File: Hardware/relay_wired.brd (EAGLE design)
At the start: 100 x 80 mm, 9 parts, among them K1 JJM1-12V

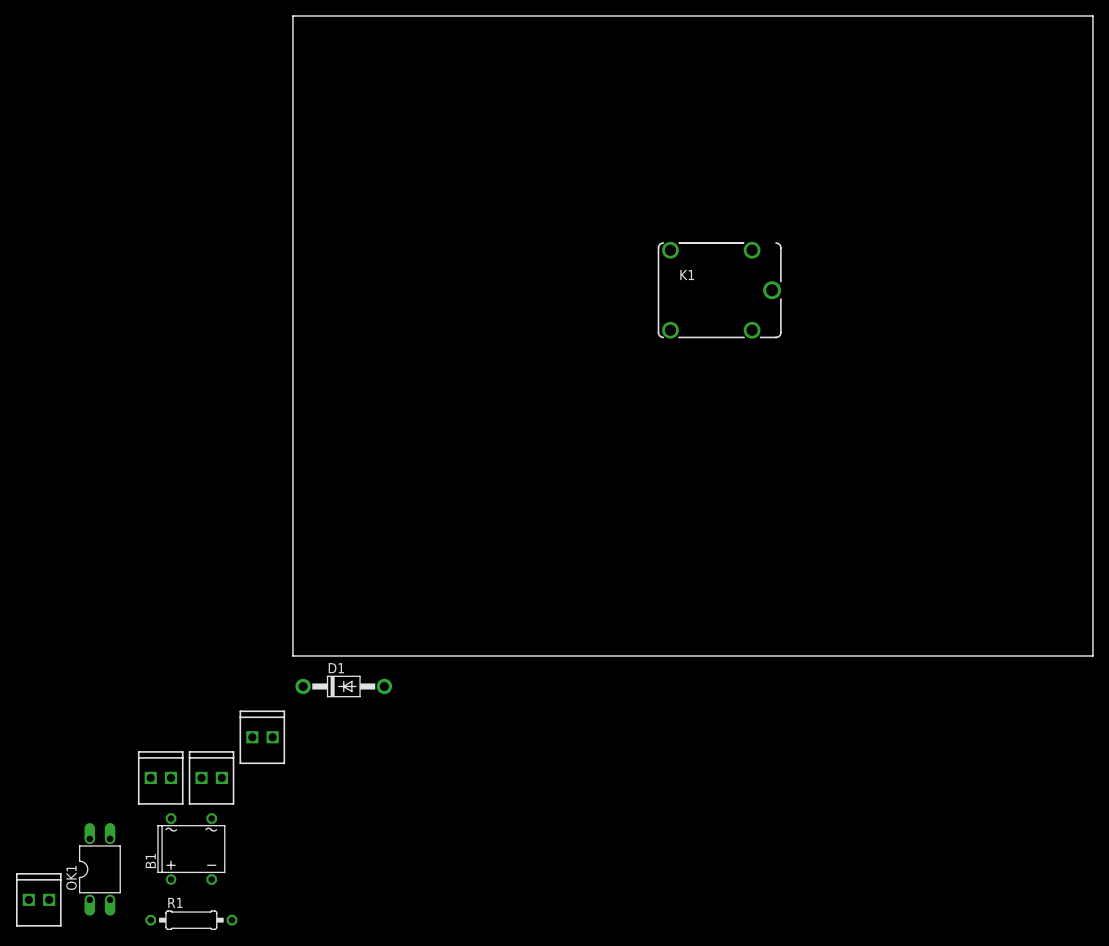
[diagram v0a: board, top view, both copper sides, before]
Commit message: Layout of board 33 x 33
Layout 33 x 33 board
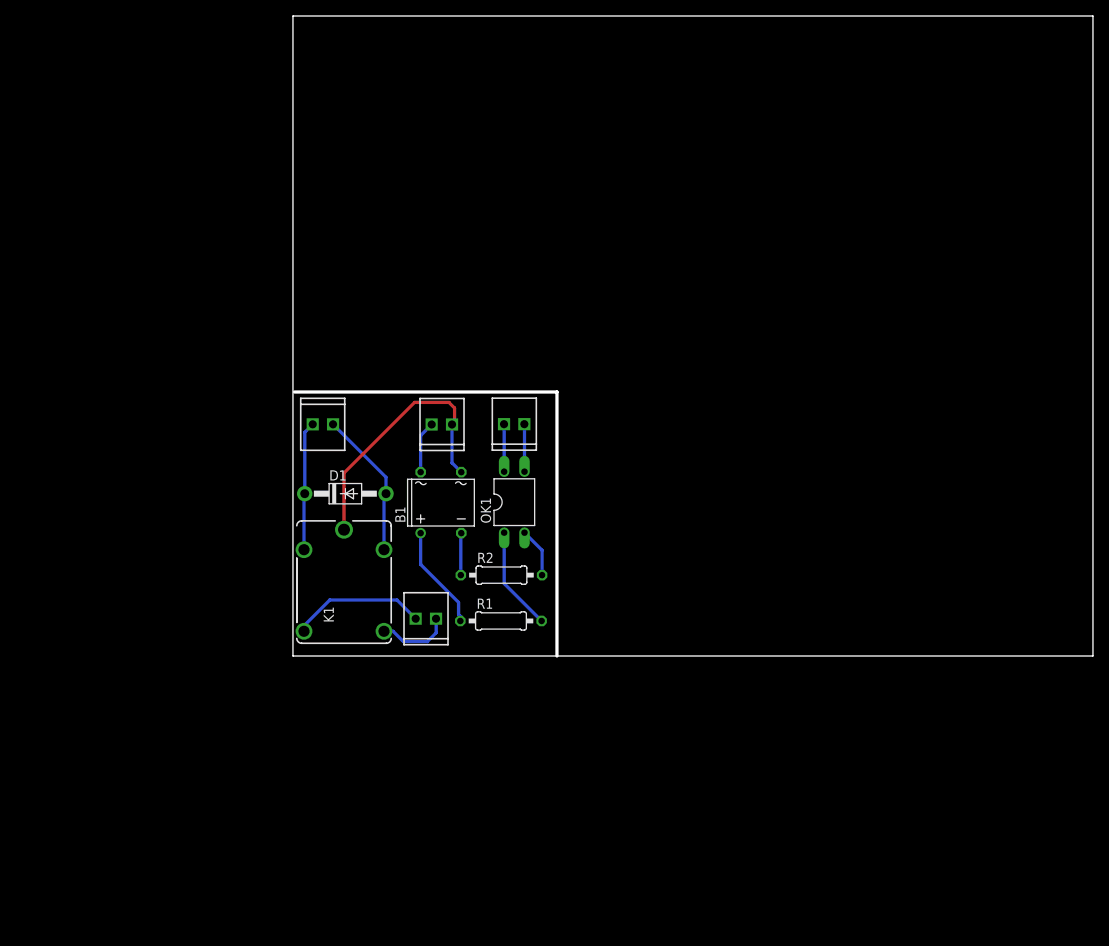
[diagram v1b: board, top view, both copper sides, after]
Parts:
- added R2: (no value), resistor:0207/10
- moved S/GND 85.9 mm to (28.9, 29.0), turned to 180 degrees
- moved OK1 69.2 mm to (27.7, 19.2)
- moved K1 59.5 mm to (6.38, 9.24), turned to 90 degrees
- moved LOAD/L 58.1 mm to (19.9, 28.9), turned to 180 degrees
- moved R1 53.8 mm to (26.0, 4.38)
- moved B1 53.4 mm to (18.5, 19.2)
- moved 12V/BJT 46.3 mm to (2.47, 29.0)
- moved NO/NC 27.3 mm to (17.9, 4.66), turned to 180 degrees
- moved D1 24.1 mm to (6.55, 20.3)
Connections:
- new net N$10: OK1.2, R2.2
- net N$8: now also R2.1; no longer OK1.2
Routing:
- net N$3: track 0.00 -> 33.5 mm
- net N$2: track 0.00 -> 18.5 mm
- net N$5: track 0.00 -> 17.0 mm
- net N$1: track 0.00 -> 16.1 mm
- net N$9: track 0.00 -> 13.1 mm
- net N$6: track 0.00 -> 13.0 mm
- net N$4: track 0.00 -> 9.28 mm
- net N$7: track 0.00 -> 6.53 mm
- net N$10: track 0.00 -> 6.22 mm
- net N$12: track 0.00 -> 5.95 mm
- net N$11: track 0.00 -> 5.95 mm
- net N$8: track 0.00 -> 5.27 mm
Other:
- outline, holes or cut-outs redrawn

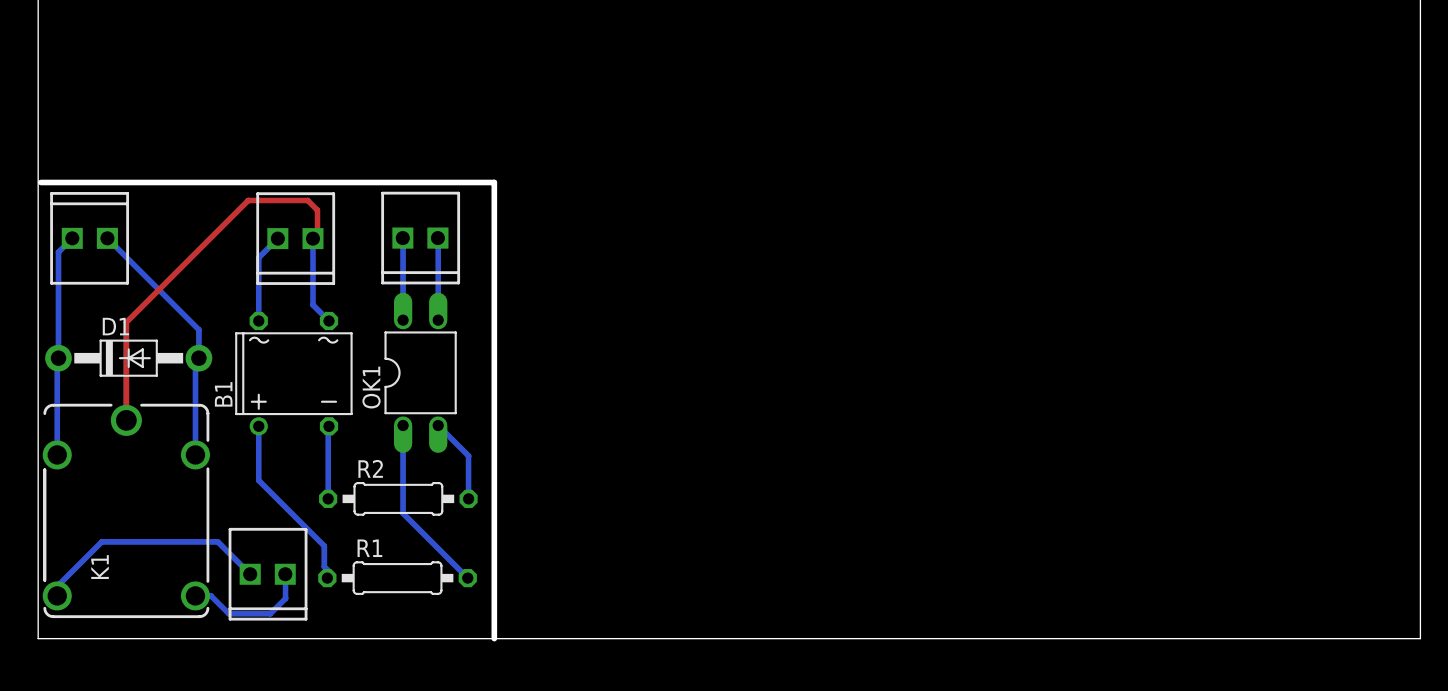
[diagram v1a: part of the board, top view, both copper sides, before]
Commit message: Change layout to 25x40mm
- Change the layout to 25x40 mm since the max board size in the free eagle version is 160mm2 (100x80)
- Added text on pcb board layout and fixed trace width
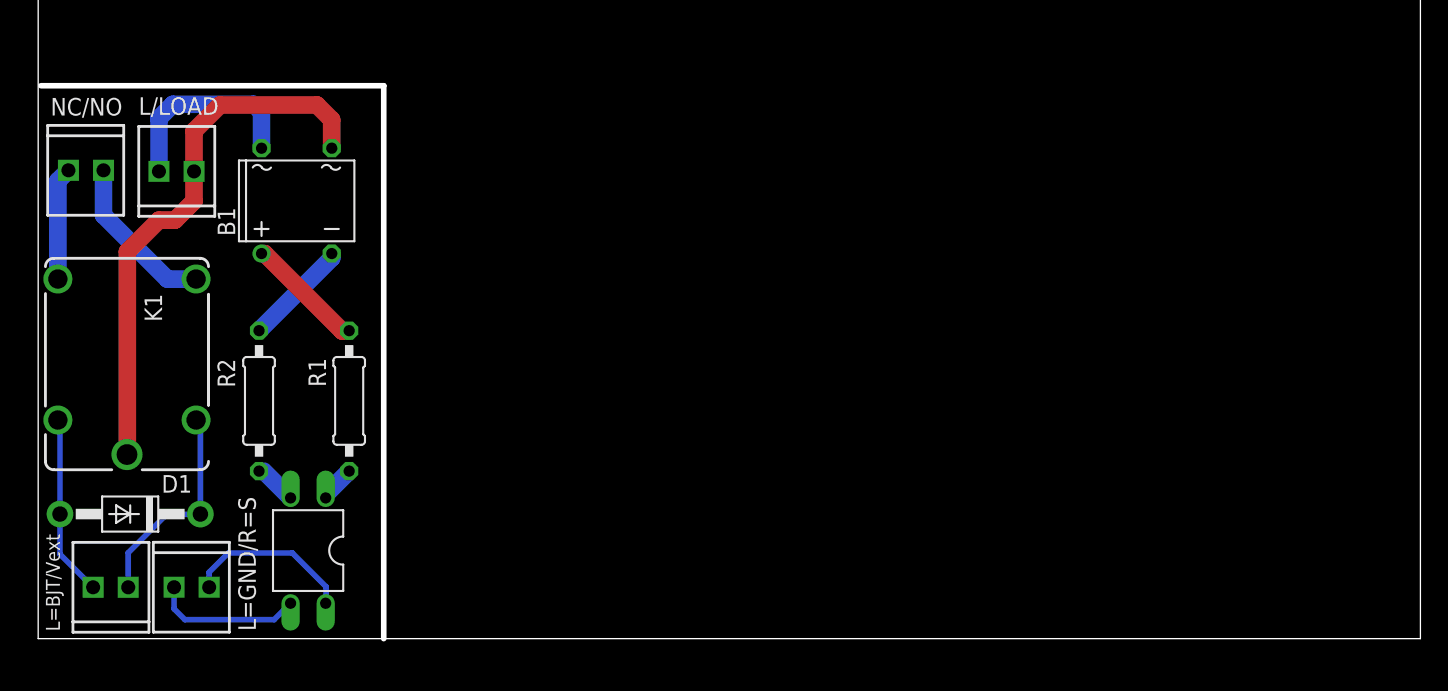
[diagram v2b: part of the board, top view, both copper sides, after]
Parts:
- D1: value 1N4004 -> 1N4007
- NO/NC: value (none) -> NO/NC
- moved NO/NC 33.2 mm to (2.19, 33.9), turned to 0 degrees
- moved S/GND 31.7 mm to (9.83, 3.72), turned to 0 degrees
- moved 12V/BJT 25.6 mm to (6.52, 3.71), turned to 180 degrees
- moved OK1 15.2 mm to (19.5, 6.37), turned to 180 degrees
- moved R1 13.3 mm to (22.5, 17.2), turned to 270 degrees
- moved B1 12.5 mm to (18.7, 31.7)
- moved R2 12.3 mm to (16.0, 17.2), turned to 270 degrees
- moved D1 11.3 mm to (6.66, 9.01), turned to 180 degrees
- moved K1 10.6 mm to (6.42, 19.9), turned to 270 degrees
- moved LOAD/L 9.88 mm to (11.3, 33.8)
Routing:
- net N$6: track 13.0 -> 2.64 mm
- net N$7: track 6.53 -> 14.5 mm
- net N$11: track 5.95 -> 12.3 mm
- net N$3: track 33.5 -> 39.3 mm
- net N$2: track 18.5 -> 13.2 mm
- net N$5: track 17.0 -> 11.9 mm
- net N$12: track 5.95 -> 10.8 mm
- net N$9: track 13.1 -> 8.68 mm
- net N$10: track 6.22 -> 3.09 mm
- net N$8: track 5.27 -> 7.76 mm
- net N$4: track 9.28 -> 8.18 mm
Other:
- outline, holes or cut-outs redrawn
- board text added: "L/LOAD"
- board text added: "L=BJT/Vext"
- board text added: "L=GND/R=S"
- board text added: "NC/NO"

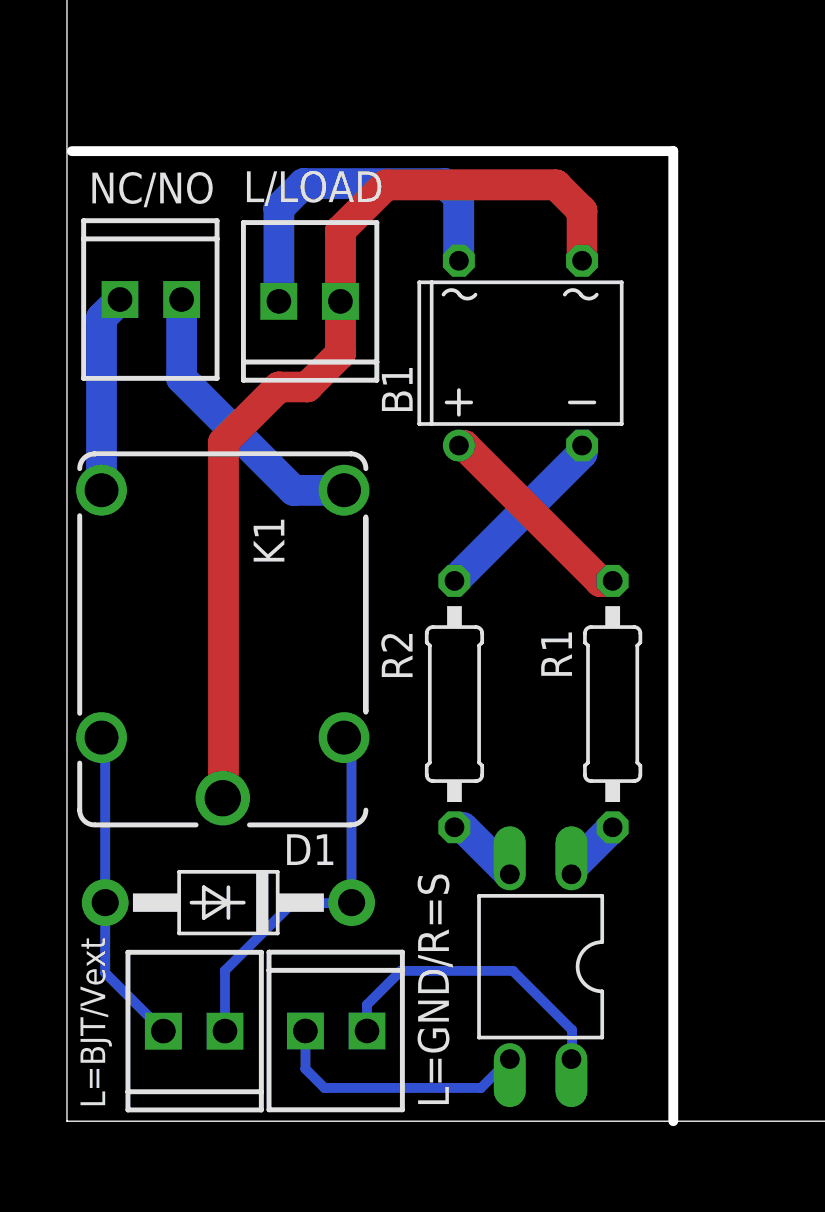
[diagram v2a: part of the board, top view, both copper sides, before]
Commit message: Branch for new design using SFH620A
Due to design layout size limitation - after fixing parts size - it was not possible to fit in the 25x40 layout a pc817 and a DB107 for detecting zero crossing. Thus this branch is to replace both with the SFH620A IC instead.

- Changed the terminal block size from 2.54 mm to 5 mm pith instead since this was available in the market.
- Changed the relay to SONGLE SRD-05VDC-SL-C design. Library is added also
- Changed resistors value to 0207/12 to fit 22k / 1W resistor value.
- Changed pic817 and DB107 with SFH620A
- reroute pcb layout again.

Todo: 
- Creepage 
- Double layer for high voltage side.
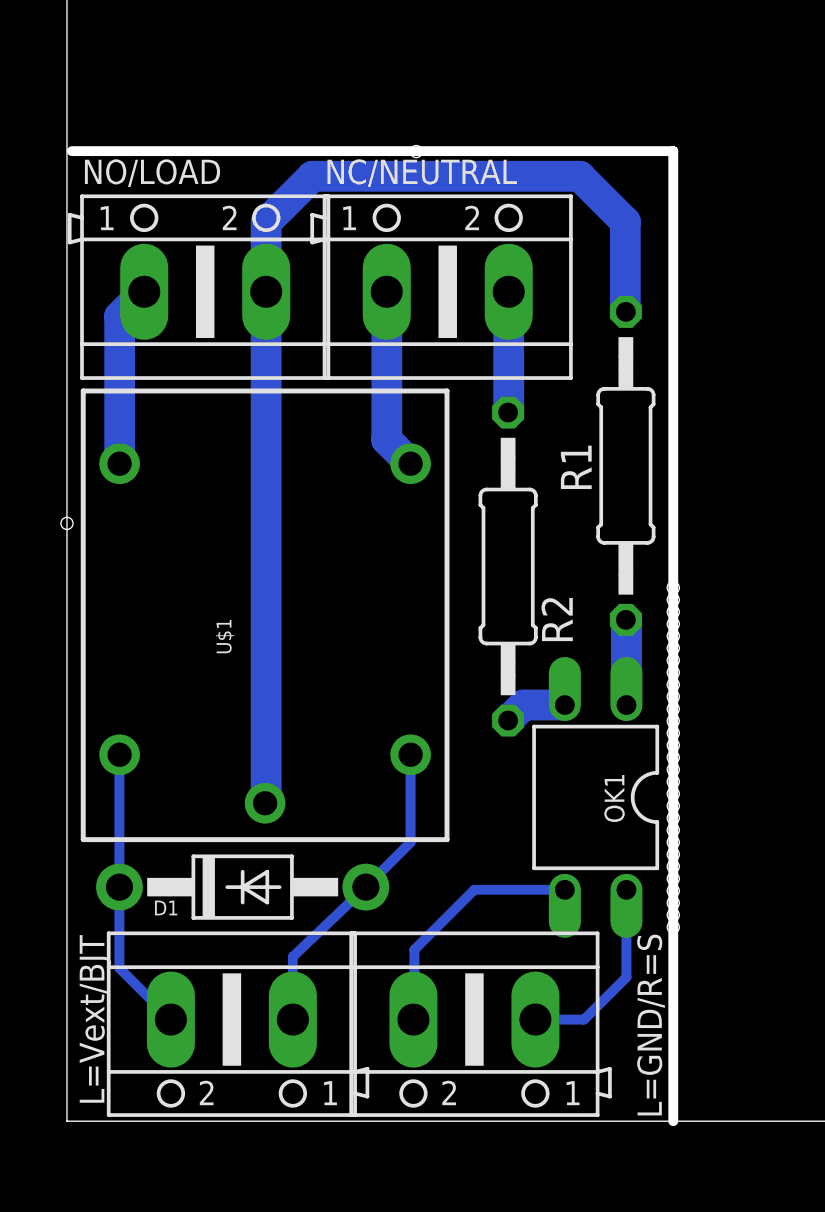
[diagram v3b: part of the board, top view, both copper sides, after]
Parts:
- removed 12V/BJT, LOAD/L, S/GND: (no value), SparkFun-Connectors:1X02_2.54_SCREWTERM
- removed B1: DBDB107G, rectifier:DB
- removed K1: JJM1-12V, relay:JJM1C
- removed NO/NC: NO/NC, SparkFun-Connectors:1X02_2.54_SCREWTERM
- added GND/S, NC/NEUTRAL, NO/LOAD, VEXT/BJT: (no value), con-ptr500:AK500/2
- added U$1: RELAYPTH, SRD-05VDC-SL-C:SRD-05VDC-SL-C
- OK1: value PC817 -> SFH620A
- R1, R2: value (none) -> 22k/1W; device resistor:0207/10 -> rcl:0207/12
- moved R1 9.84 mm to (23.0, 27.0)
- moved OK1 7.34 mm to (21.8, 13.3)
- moved R2 6.09 mm to (18.2, 22.9)
- moved D1 0.87 mm to (7.24, 9.65), turned to 0 degrees
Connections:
- removed net N$5 (its old number): K1.NO, NO/NC.P1
- removed net N$7: B1.AC2, LOAD/L.P1
- removed net N$8: B1.-, R2.1
- new net N$13: D1.A, U$1.COIL0, VEXT/BJT.1
- net N$1: now also U$1.COIL1, VEXT/BJT.2; no longer 12V/BJT.P2, K1.1
- net N$11: now also GND/S.1; no longer S/GND.P1
- net N$12: now also GND/S.2; no longer S/GND.P2
- net N$2: now also NC/NEUTRAL.1, U$1.SWCLOSED; no longer 12V/BJT.P1, D1.A, K1.2
- net N$3: now also NO/LOAD.1, U$1.SWOPEN; no longer B1.AC1, K1.C, LOAD/L.P2
- net N$4: now also NC/NEUTRAL.2, R2.1; no longer K1.NC, NO/NC.P2
- net N$9: now also NO/LOAD.2, U$1.SWCOMMON; no longer B1.+
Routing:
- net N$9: track 8.68 -> 44.1 mm
- net N$3: track 39.3 -> 7.51 mm
- net N$7: track 14.5 -> 0.00 mm
- net N$13: track 0.00 -> 13.0 mm
- net N$5 (its old number): track 11.9 -> 0.00 mm
- net N$8: track 7.76 -> 0.00 mm
- net N$2: track 13.2 -> 7.50 mm
- net N$11: track 12.3 -> 8.08 mm
- net N$1: track 15.8 -> 11.8 mm
- net N$4: track 8.18 -> 4.99 mm
- net N$6: track 2.64 -> 3.52 mm
- net N$12: track 10.8 -> 10.1 mm
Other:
- board text added: "L=Vext/BJT"
- board text removed: "L/LOAD"
- board text removed: "L=BJT/Vext"
- board text removed: "NC/NO"

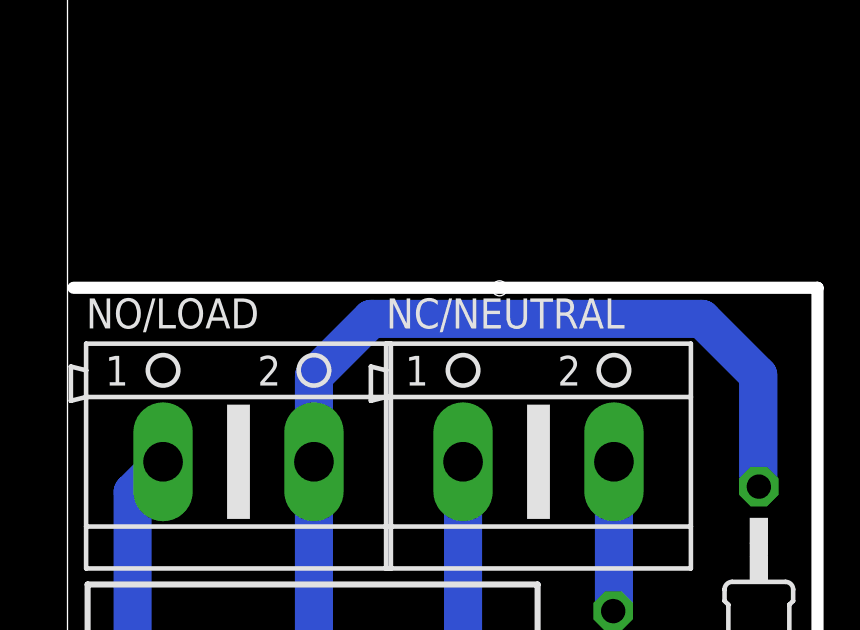
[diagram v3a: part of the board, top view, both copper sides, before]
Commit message: Invert NC and NO name tags
Changes in schematic.
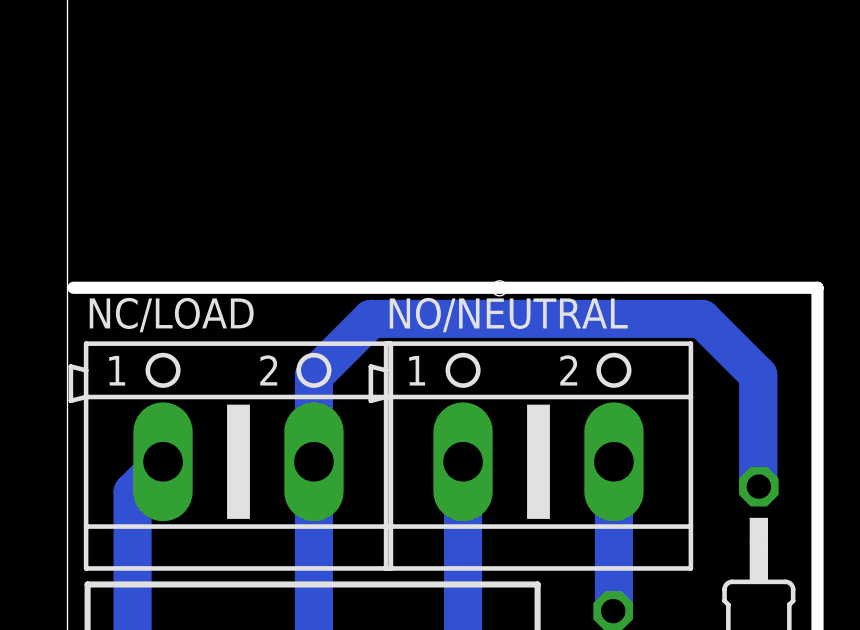
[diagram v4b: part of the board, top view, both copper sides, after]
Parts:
- renumbered NC/NEUTRAL to NO/NEUTRAL, NO/LOAD to NC/LOAD
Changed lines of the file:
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@@
 <attribute name="VALUE" x="17.5552" y="25.1328" size="0.8128" layer="27" ratio="10" rot="R270"/>
 </element>
-<element name="NO/LOAD" library="con-ptr500" package="AK500/2" value="" x="5.7" y="34.2" smashed="yes">
+<element name="NC/LOAD" library="con-ptr500" package="AK500/2" value="" x="5.7" y="34.2" smashed="yes">
 <attribute name="OC_NEWARK" value="unknown" x="5.7" y="34.2" size="1.778" layer="27" display="off"/>
 <attribute name="MF" value="" x="5.7" y="34.2" size="1.778" layer="27" display="off"/>
@@
 <attribute name="VALUE" x="11.88" y="9.906" size="1.778" layer="27" ratio="10" rot="R180"/>
 </element>
-<element name="NC/NEUTRAL" library="con-ptr500" package="AK500/2" value="" x="15.7" y="34.2" smashed="yes">
+<element name="NO/NEUTRAL" library="con-ptr500" package="AK500/2" value="" x="15.7" y="34.2" smashed="yes">
 <attribute name="OC_NEWARK" value="unknown" x="15.7" y="34.2" size="1.778" layer="27" display="off"/>
 <attribute name="MF" value="" x="15.7" y="34.2" size="1.778" layer="27" display="off"/>
@@
 <contactref element="R1" pad="1"/>
 <contactref element="U$1" pad="SWCOMMON"/>
-<contactref element="NO/LOAD" pad="2"/>
+<contactref element="NC/LOAD" pad="2"/>
 <wire x1="8.2146" y1="34.2" x2="8.2146" y2="13.1546" width="1.27" layer="16"/>
 <wire x1="8.2146" y1="13.1546" x2="8.17" y2="13.11" width="1.27" layer="16"/>
@@
 <signal name="N$3">
 <contactref element="U$1" pad="SWOPEN"/>
-<contactref element="NO/LOAD" pad="1"/>
+<contactref element="NC/LOAD" pad="1"/>
 <wire x1="2.17" y1="27.11" x2="2.17" y2="33.1846" width="1.27" layer="16"/>
 <wire x1="2.17" y1="33.1846" x2="3.1854" y2="34.2" width="1.27" layer="16"/>
@@
 <signal name="N$4">
 <contactref element="R2" pad="1"/>
-<contactref element="NC/NEUTRAL" pad="2"/>
+<contactref element="NO/NEUTRAL" pad="2"/>
 <wire x1="18.2146" y1="34.2" x2="18.2146" y2="29.2466" width="1.27" layer="16"/>
 <wire x1="18.2146" y1="29.2466" x2="18.1902" y2="29.2222" width="1.27" layer="16"/>
@@
 <signal name="N$2">
 <contactref element="U$1" pad="SWCLOSED"/>
-<contactref element="NC/NEUTRAL" pad="1"/>
+<contactref element="NO/NEUTRAL" pad="1"/>
 <wire x1="13.1854" y1="34.2" x2="13.1854" y2="28.0946" width="1.27" layer="16"/>
 <wire x1="13.1854" y1="28.0946" x2="14.17" y2="27.11" width="1.27" layer="16"/>
